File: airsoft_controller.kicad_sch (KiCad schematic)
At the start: 25 parts

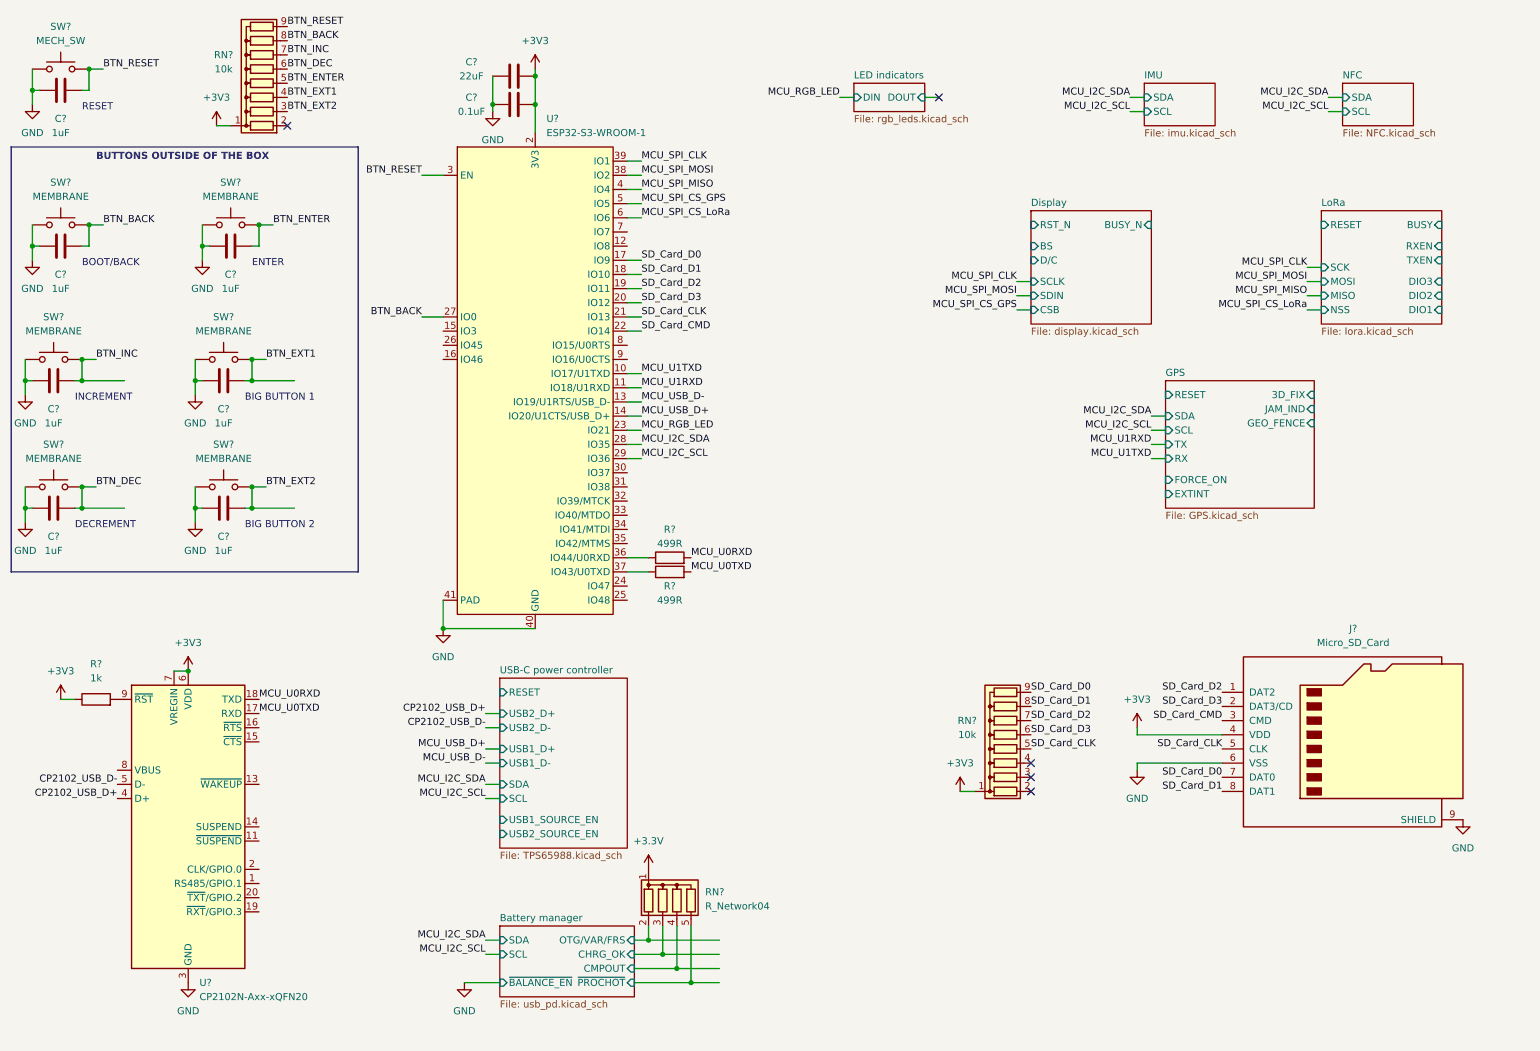
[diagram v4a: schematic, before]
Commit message: added audio ref schematic, added bat to 5V, added shift register, connected devices with other periferals
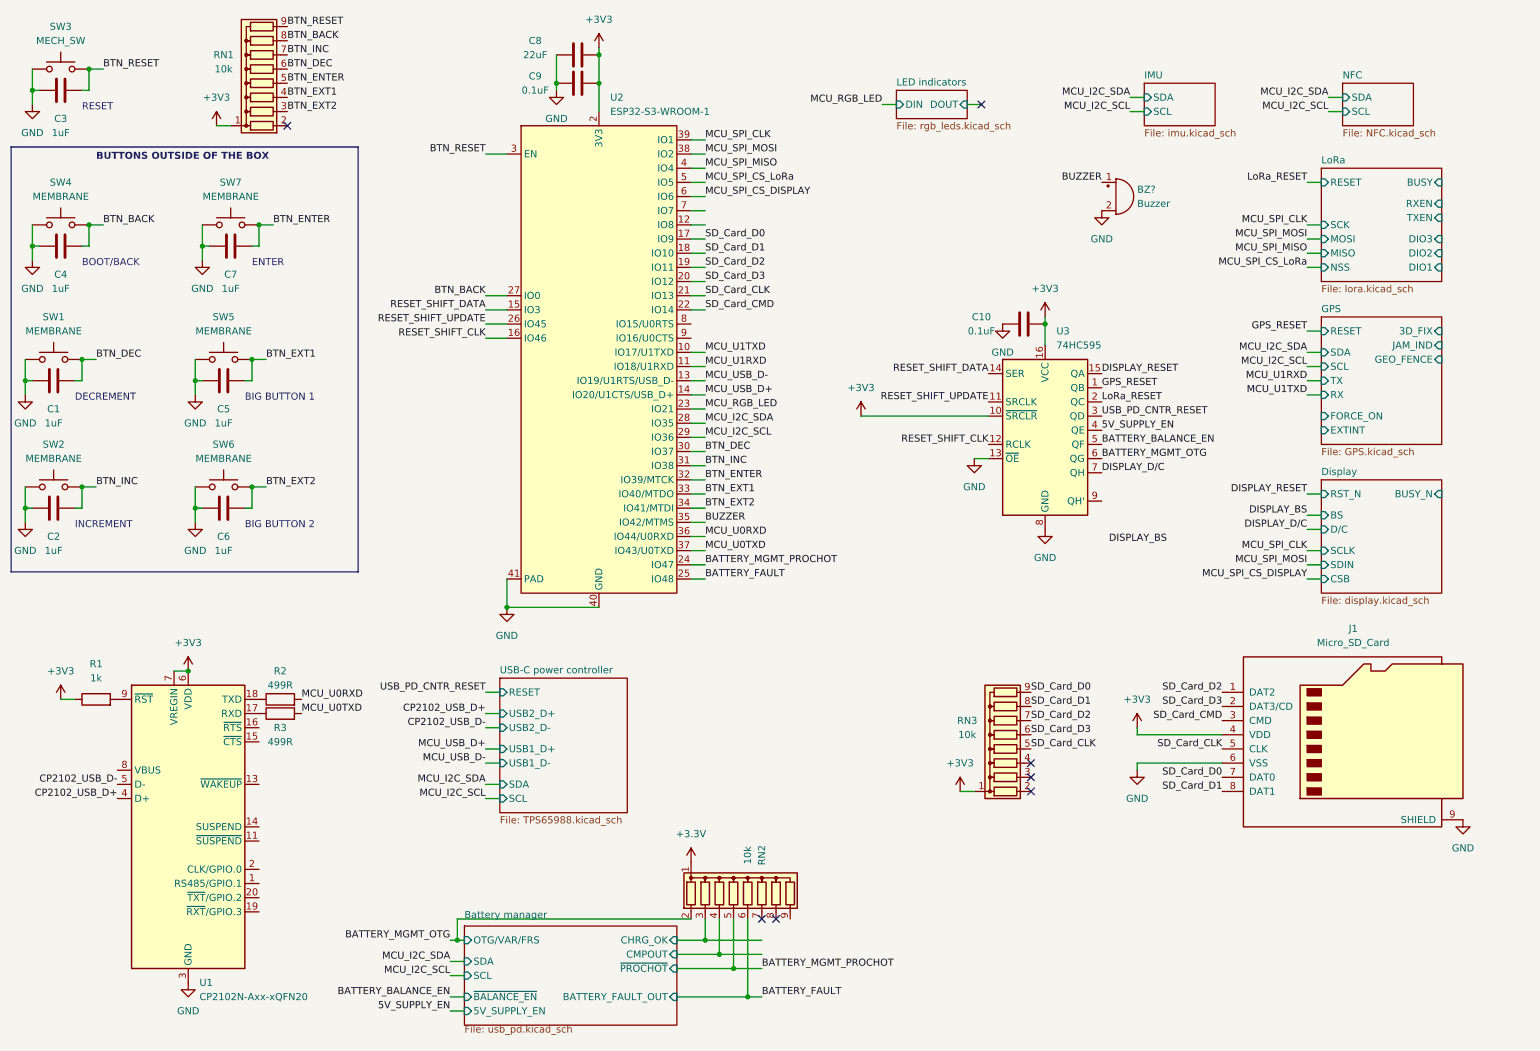
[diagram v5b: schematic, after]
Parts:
- removed RN?: R_Network04, Resistor_THT:R_Array_SIP5, symbol Device:R_Network04
- added BZ?: Buzzer, symbol Device:Buzzer
- added C10: 0.1uF, symbol Device:C
- added RN2: 10k, Resistor_THT:R_Array_SIP9, symbol Device:R_Network08
- added U3: 74HC595, symbol 74xx:74HC595
- gave numbers to parts that had none: 24
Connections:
- net MCU_SPI_CS_GPS is gone; now on net MCU_SPI_CS_LoRa: U2.5 (IO5)
- net +3.3V: now also RN2.1 (common)
- net +3V3: now also C10.2, U3.10 (~{SRCLR}), U3.16 (VCC)
- net BTN_DEC: now also C1.1, SW1.2, U2.30 (IO37); no longer C2.1, SW2.2
- net BTN_ENTER: now also U2.32 (IO39/MTCK)
- net BTN_EXT1: now also U2.33 (IO40/MTDO)
- net BTN_EXT2: now also U2.34 (IO41/MTDI)
- net BTN_INC: now also C2.1, SW2.2, U2.31 (IO38); no longer C1.1, SW1.2
- net Battery manager/CHRG_OK: now also RN2.3 (R2)
- net Battery manager/CMPOUT: now also RN2.4 (R3)
- net GND: now also BZ?.2 (+), C10.1, U3.13 (~{OE}), U3.8 (GND)
- net MCU_SPI_CS_LoRa: no longer U2.6 (IO6)
- net MCU_U0RXD: now also U2.36 (IO44/U0RXD); no longer U1.18 (TXD)
- net MCU_U0TXD: now also U2.37 (IO43/U0TXD); no longer U1.17 (RXD)
- net at R3.1: now also U1.17 (RXD); no longer U2.37 (IO43/U0TXD)
- net at R2.1: now also U1.18 (TXD); no longer U2.36 (IO44/U0RXD)
- net RESET_SHIFT_DATA: now reaches U2.15 (IO3)
- net RESET_SHIFT_DATA: now also U3.14 (SER)
- net RESET_SHIFT_CLK: now reaches U2.16 (IO46)
- net RESET_SHIFT_CLK: now also U3.12 (RCLK)
- net BATTERY_MGMT_PROCHOT: now reaches U2.24 (IO47)
- net BATTERY_MGMT_PROCHOT: now also RN2.5 (R4)
- net BATTERY_FAULT: now reaches U2.25 (IO48)
- net BATTERY_FAULT: now also RN2.6 (R5)
- net RESET_SHIFT_UPDATE: now reaches U2.26 (IO45)
- net RESET_SHIFT_UPDATE: now also U3.11 (SRCLK)
- net BUZZER: now reaches U2.35 (IO42/MTMS)
- net BUZZER: now also BZ?.1 (-)
- new net 5V_SUPPLY_EN: U3.4 (QE)
- new net BATTERY_BALANCE_EN: U3.5 (QF)
- new net BATTERY_MGMT_OTG: RN2.2 (R1), U3.6 (QG)
- new net DISPLAY_D/C: U3.7 (QH)
- new net DISPLAY_RESET: U3.15 (QA)
- new net GPS_RESET: U3.1 (QB)
- new net LoRa_RESET: U3.2 (QC)
- new net MCU_SPI_CS_DISPLAY: U2.6 (IO6)
- new net USB_PD_CNTR_RESET: U3.3 (QD)
- no-connect marks 5 -> 7
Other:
- sheet Battery manager ports: added 5V_SUPPLY_EN, BATTERY_FAULT_OUT; removed none
- sheet USB-C power controller ports: added none; removed USB1_SOURCE_EN, USB2_SOURCE_EN
- moved on the sheet: C8, C9, R2, R3, U2

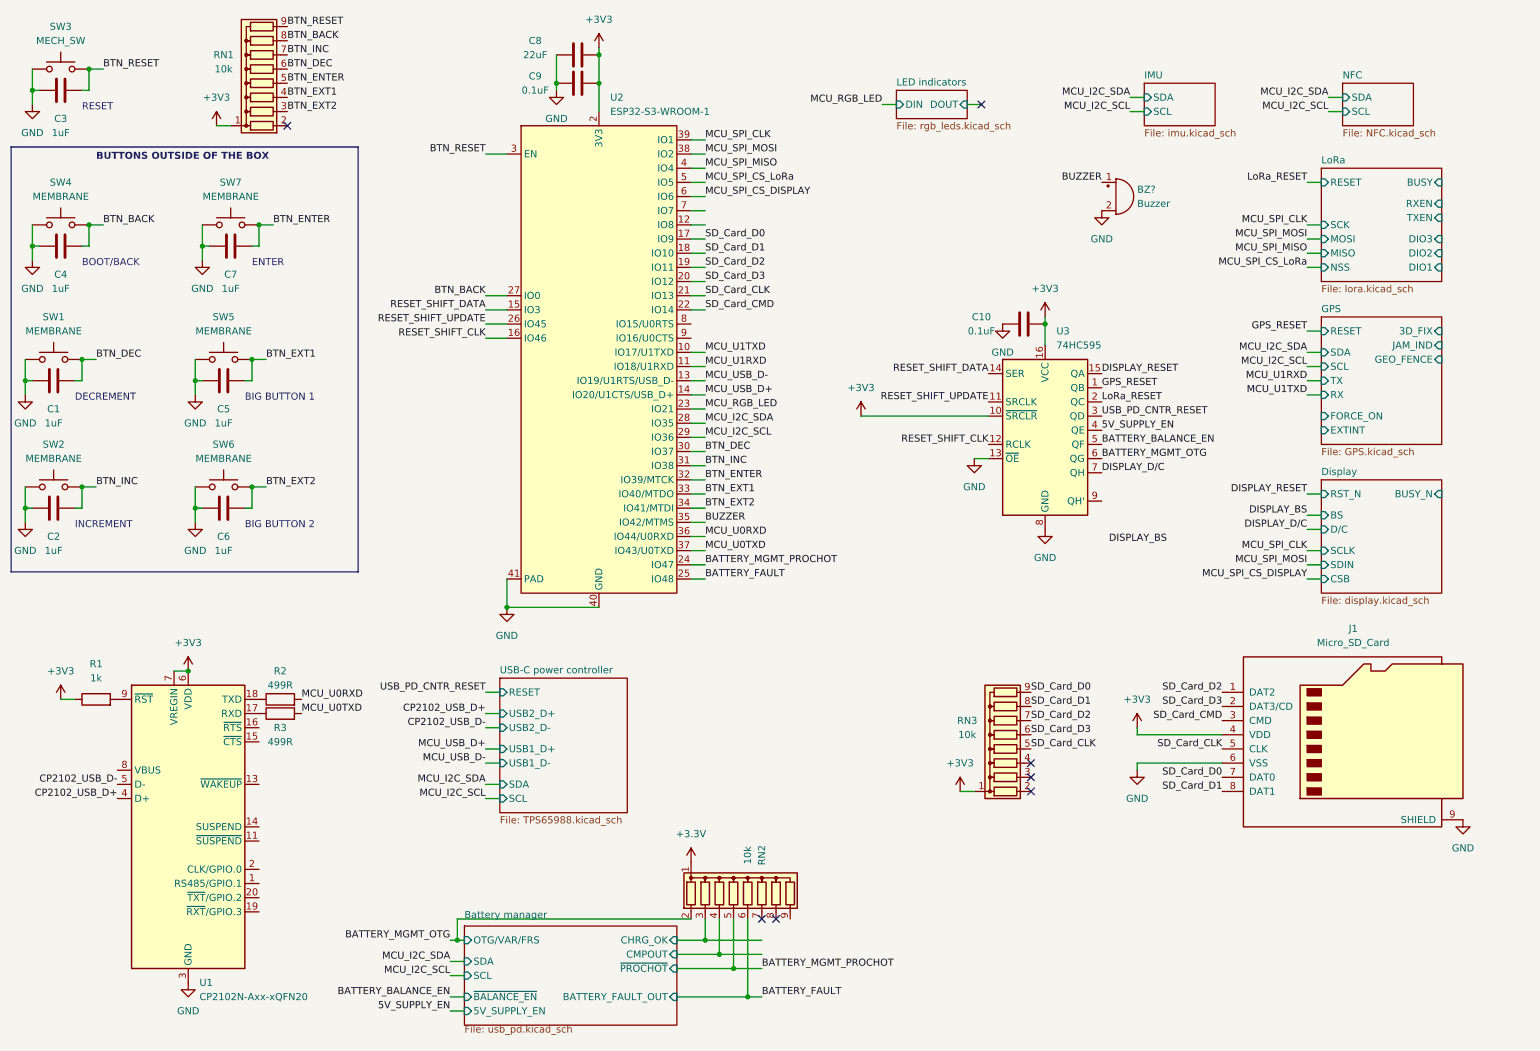
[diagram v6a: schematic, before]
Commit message: added adcin2 config description, fixed some rule check errors
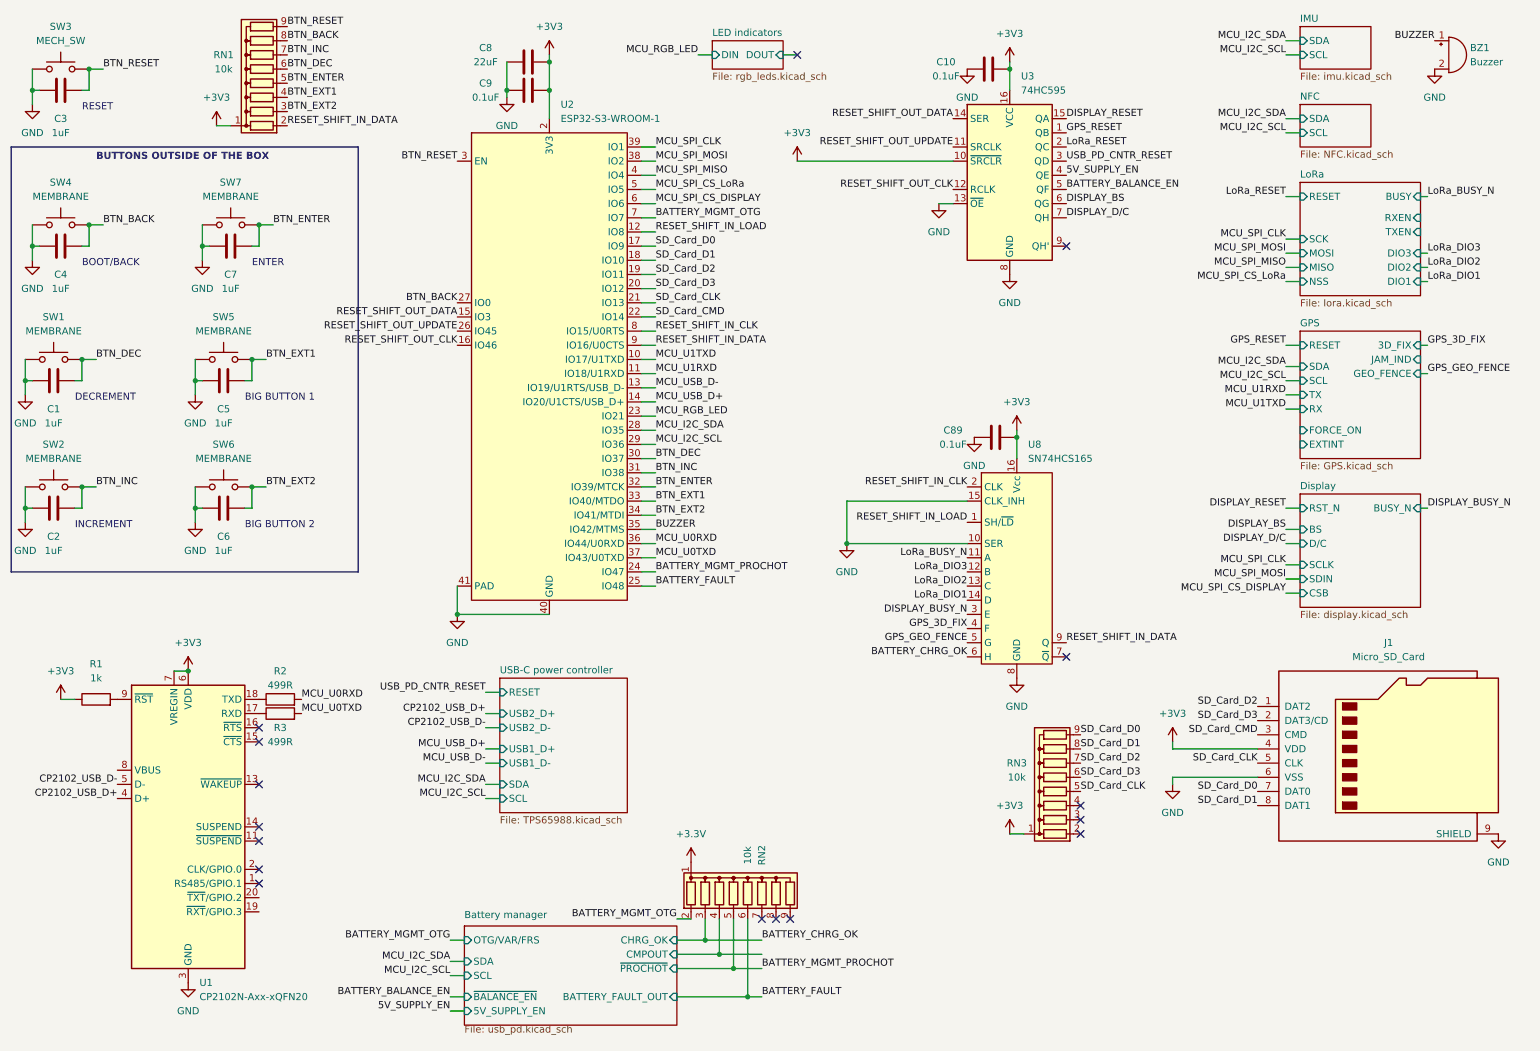
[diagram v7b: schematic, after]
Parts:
- added C89: 0.1uF, symbol Device:C
- added U8: SN74HCS165, symbol airsoft_controller:SN74HCS165
- gave numbers to parts that had none: 1
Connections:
- net +3V3: now also C89.2, U8.16 (Vcc)
- net BATTERY_MGMT_OTG: now also U2.7 (IO7); no longer U3.6 (QG)
- net DISPLAY_BS: now also U3.6 (QG)
- net GND: now also C89.1, U8.10 (SER), U8.15 (CLK_INH), U8.8 (GND)
- net RESET_SHIFT_IN_DATA: now reaches RN1.2 (R1)
- net RESET_SHIFT_IN_DATA: now also U2.9 (IO16/U0CTS), U8.9 (Q)
- net RESET_SHIFT_IN_LOAD: now reaches U2.12 (IO8)
- net RESET_SHIFT_IN_LOAD: now also U8.1 (SH/~{LD})
- net RESET_SHIFT_IN_CLK: now reaches U2.8 (IO15/U0RTS)
- net RESET_SHIFT_IN_CLK: now also U8.2 (CLK)
- net Battery manager/CHRG_OK renamed BATTERY_CHRG_OK
- net BATTERY_CHRG_OK: now also U8.6 (H)
- net RESET_SHIFT_CLK renamed RESET_SHIFT_OUT_CLK
- net RESET_SHIFT_DATA renamed RESET_SHIFT_OUT_DATA
- net RESET_SHIFT_UPDATE renamed RESET_SHIFT_OUT_UPDATE
- new net DISPLAY_BUSY_N: U8.3 (E)
- new net GPS_3D_FIX: U8.4 (F)
- new net GPS_GEO_FENCE: U8.5 (G)
- new net LoRa_BUSY_N: U8.11 (A)
- new net LoRa_DIO1: U8.14 (D)
- new net LoRa_DIO2: U8.13 (C)
- new net LoRa_DIO3: U8.12 (B)
- no-connect marks 7 -> 16
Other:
- moved on the sheet: BZ1, C10, C8, C9, J1, RN3, U2, U3

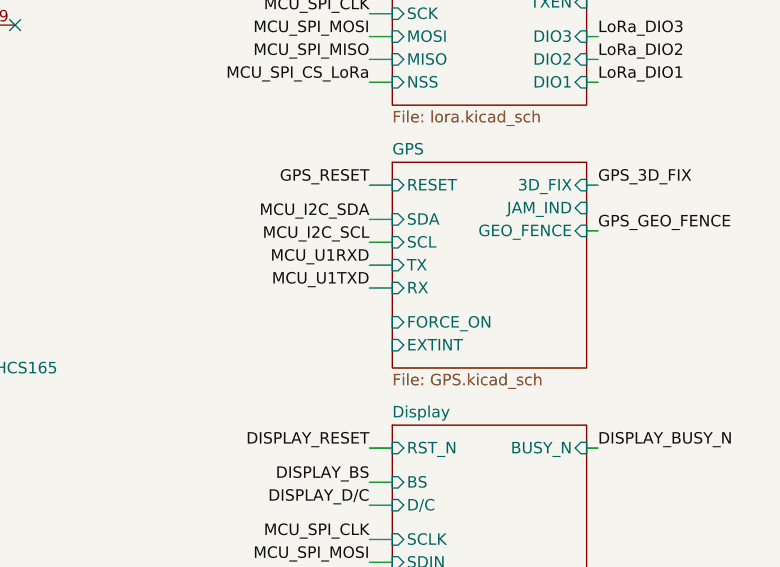
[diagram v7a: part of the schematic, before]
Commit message: added external connectors
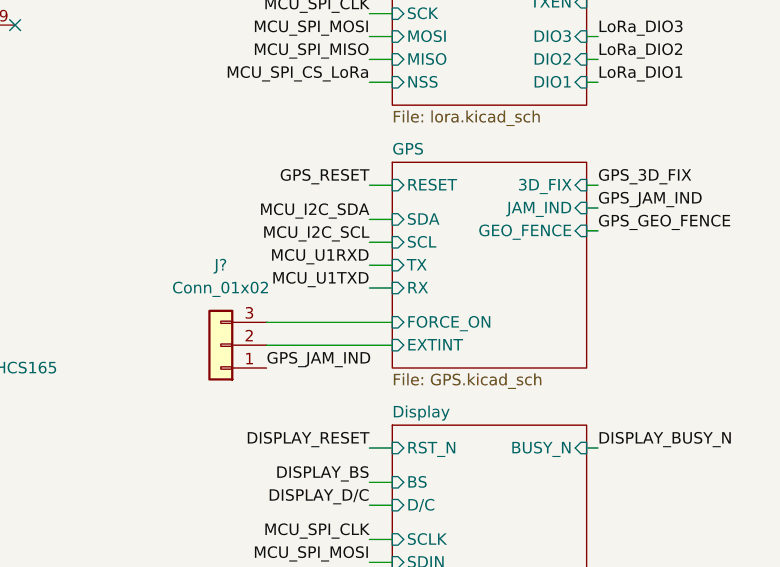
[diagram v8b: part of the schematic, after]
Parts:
- added J?: Conn_01x02, symbol Connector_Generic:Conn_01x03
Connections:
- net GPS/EXTINT: now also J?.2 (Pin_2)
- net GPS/FORCE_ON: now also J?.3 (Pin_3)
- new net GPS_JAM_IND: J?.1 (Pin_1)
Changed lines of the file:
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@@
     (stroke (width 0) (type default) (color 0 0 0 0))
   )
+  (wire (pts (xy 232.41 87.63) (xy 246.38 87.63))
+    (stroke (width 0) (type default) (color 0 0 0 0))
+  )
   (wire (pts (xy 130.81 44.45) (xy 128.27 44.45))
     (stroke (width 0) (type default) (color 0 0 0 0))
@@
     (stroke (width 0) (type default) (color 0 0 0 0))
   )
+  (wire (pts (xy 232.41 90.17) (xy 246.38 90.17))
+    (stroke (width 0) (type default) (color 0 0 0 0))
+  )
   (wire (pts (xy 49.53 54.61) (xy 49.53 50.8))
     (stroke (width 0) (type default) (color 0 0 0 0))
@@
     (stroke (width 0) (type default) (color 0 0 0 0))
   )
+  (wire (pts (xy 267.97 74.93) (xy 269.24 74.93))
+    (stroke (width 0) (type default) (color 0 0 0 0))
+  )
   (wire (pts (xy 130.81 85.09) (xy 128.27 85.09))
     (stroke (width 0) (type default) (color 0 0 0 0))
@@
     (effects (font (size 1.27 1.27)) (justify right bottom))
   )
+  (label "GPS_JAM_IND" (at 232.41 92.71 0)
+    (effects (font (size 1.27 1.27)) (justify left bottom))
+  )
   (label "MCU_I2C_SCL" (at 243.84 78.74 180)
     (effects (font (size 1.27 1.27)) (justify right bottom))
@@
     (effects (font (size 1.27 1.27)) (justify right bottom))
   )
+  (label "GPS_JAM_IND" (at 269.24 74.93 0)
+    (effects (font (size 1.27 1.27)) (justify left bottom))
+  )
   (label "SD_Card_D0" (at 207.01 142.24 0)
     (effects (font (size 1.27 1.27)) (justify left bottom))
@@
     (pin "2")
   )
+  (symbol (lib_id "Connector_Generic:Conn_01x03") (at 227.33 90.17 180) (unit 1)
+    (in_bom yes) (on_board yes) (fields_autoplaced)
+    (property "Reference" "J?" (id 0) (at 227.33 81.28 0))
+    (property "Value" "Conn_01x02" (id 1) (at 227.33 83.82 0))
+    (property "Footprint" "" (id 2) (at 227.33 90.17 0)
+      (effects (font (size 1.27 1.27)) hide)
+    )
+    (property "Datasheet" "~" (id 3) (at 227.33 90.17 0)
+      (effects (font (size 1.27 1.27)) hide)
+    )
+    (pin "1")
+    (pin "2")
+    (pin "3")
+  )
   (symbol (lib_id "Device:Buzzer") (at 273.05 20.32 0) (unit 1)
     (in_bom yes) (on_board yes) (fields_autoplaced)
@@
       (reference "J4") (unit 1) (value "Conn_01x04") (footprint "")
     )
+    (path "/0d5dfe22-e5a1-4b41-9f8a-117c8258e2c6"
+      (reference "J?") (unit 1) (value "Conn_01x02") (footprint "")
+    )
     (path "/8ab84ef1-8252-469c-850a-9e4f14e4ddfd/1b6885e8-6321-42c0-bca4-b4a7c870a10d/2e4aa483-c558-495e-96d2-72cdb149aabd"
